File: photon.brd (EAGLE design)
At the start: 41.5 x 46.4 mm, 1 part, among them J1 SF56

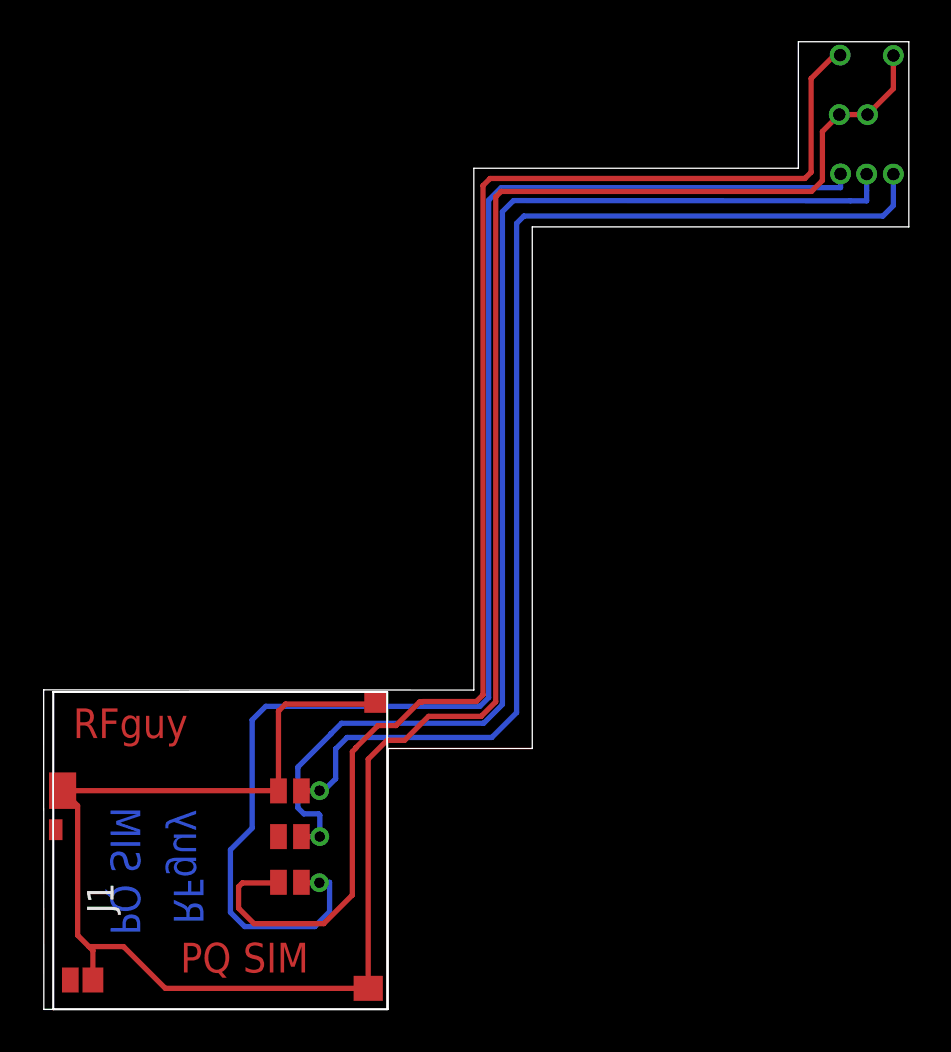
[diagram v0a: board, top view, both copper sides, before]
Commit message: New version of Board - now with correct orientation of slot
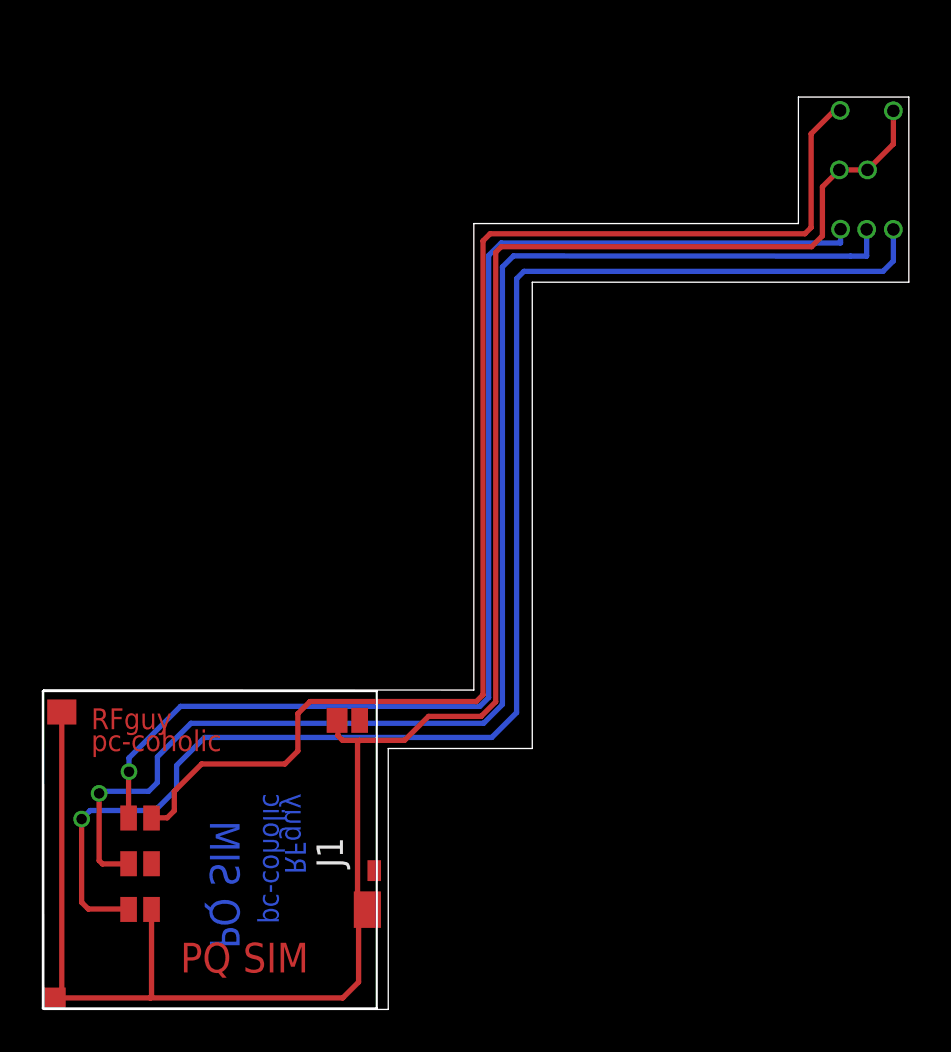
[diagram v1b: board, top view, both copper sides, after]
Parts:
- moved J1 15.5 mm to (15.8, 7.65), turned to 270 degrees
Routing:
- net C1: track 56.5 -> 71.1 mm
- net C3: track 71.4 -> 60.3 mm
- net GND: track 109.5 -> 99.9 mm
- net C2: track 58.7 -> 66.4 mm
- net C7: track 70.3 -> 64.0 mm
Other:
- board size 41.5 x 46.4 mm -> 41.5 x 43.7 mm
- board text added: "RFguy pc-coholic"
- board text removed: "RFguy"
